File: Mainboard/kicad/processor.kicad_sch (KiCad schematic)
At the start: 74 parts, among them CON1 ICD15S13E4GV00LF, IC1 STM32F765ZGT6, J1 20021521-00010D4LF, J2 SH_CON, U1 24LC64, U2 MAX7375AXR805, U3 SZNUP4114HMR6T1G, U4 SZNUP4114HMR6T1G, U5 SZNUP4114HMR6T1G, U6 SZNUP4114HMR6T1G

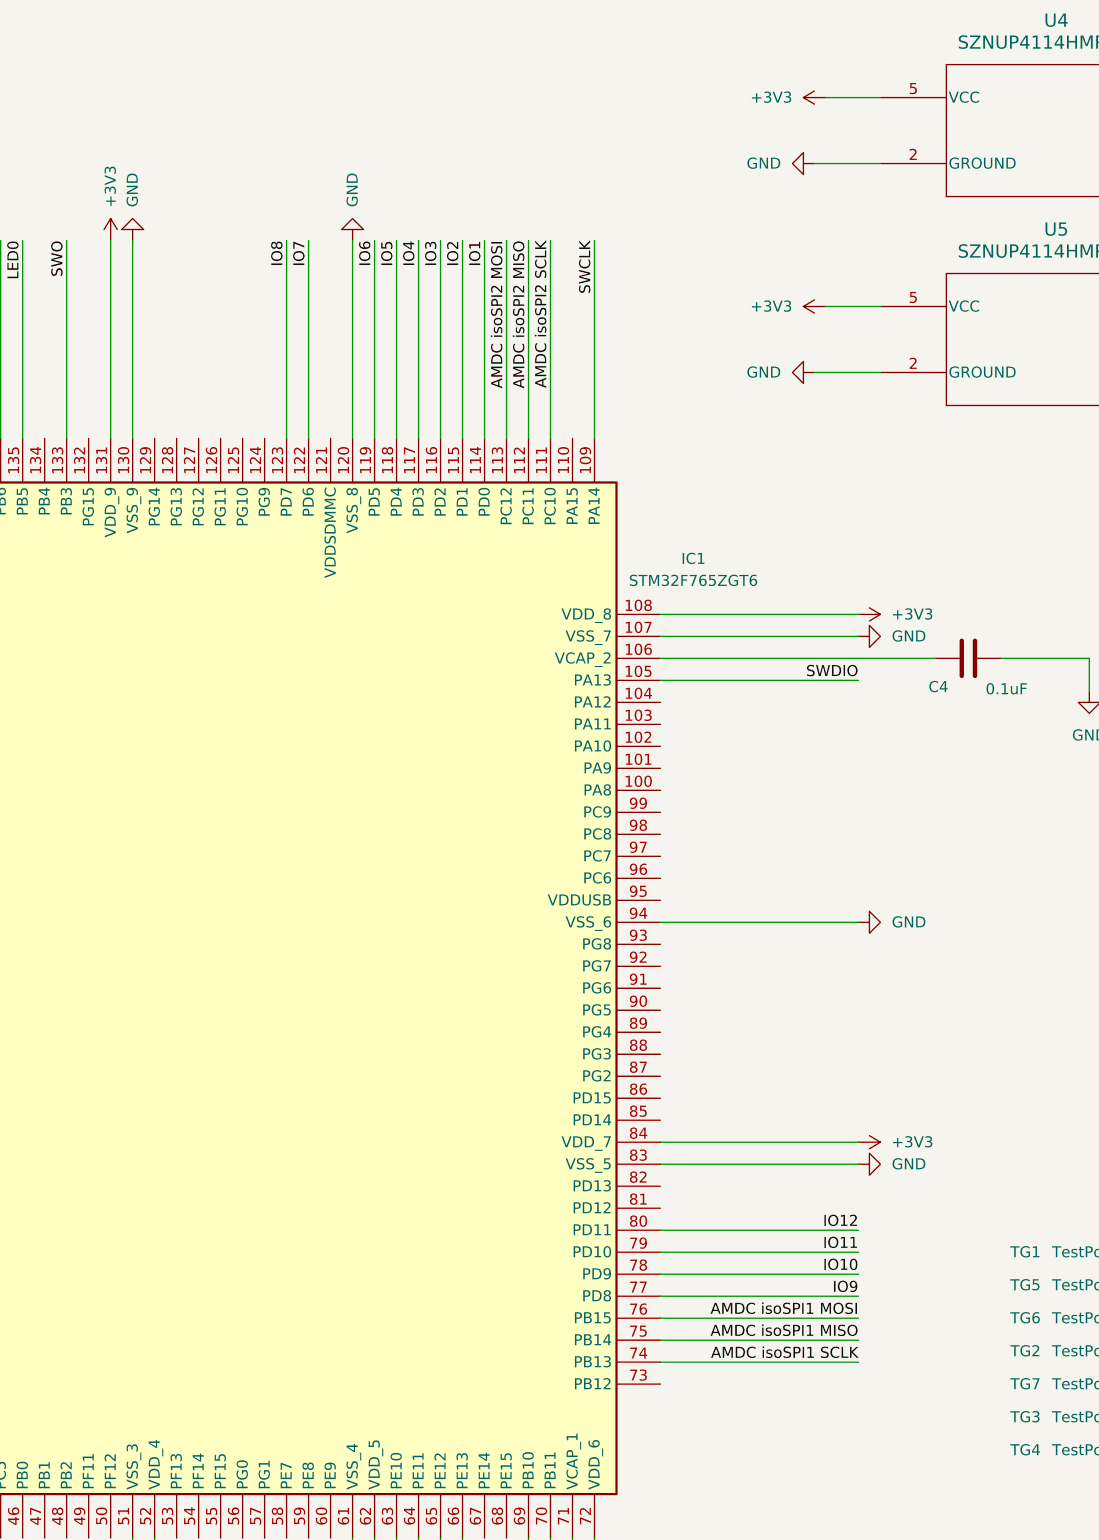
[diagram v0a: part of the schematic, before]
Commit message: Correct LED direction and processor pins
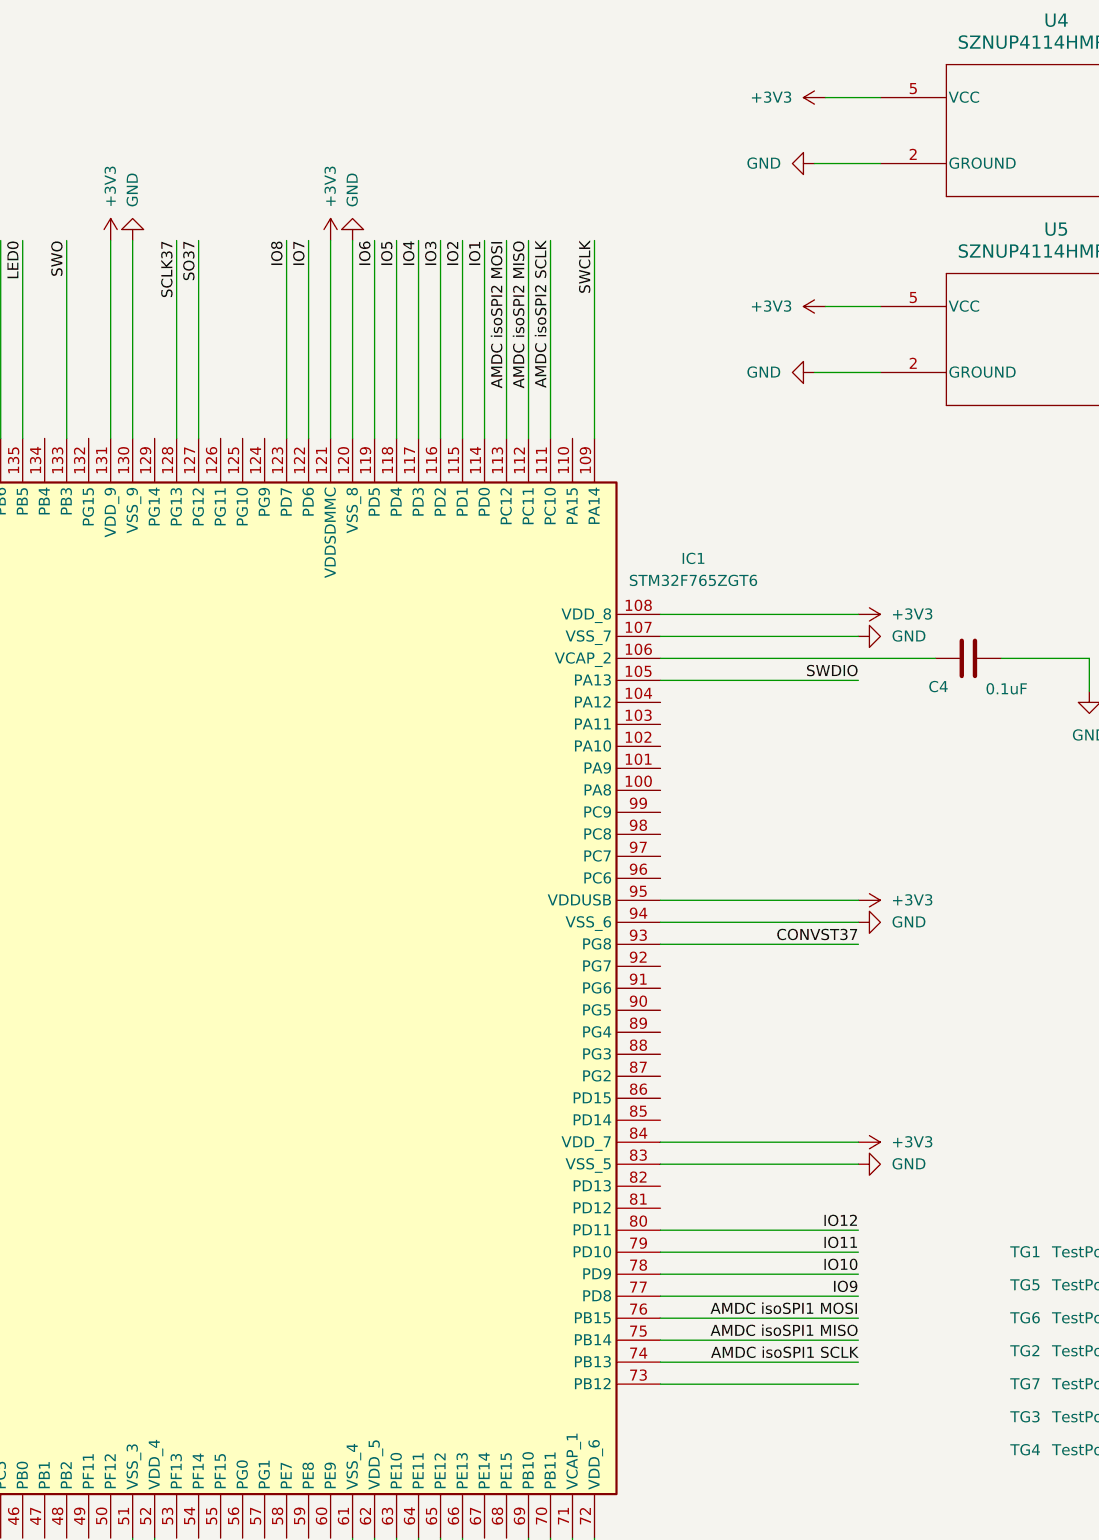
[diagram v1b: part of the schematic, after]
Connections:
- net +3V3: now also IC1.121 (VDDSDMMC), IC1.95 (VDDUSB)
- net CNVST37: now also IC1.93 (PG8)
- net SCLK37: now also IC1.128 (PG13)
- net SO37: now also IC1.127 (PG12)
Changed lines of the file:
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@@
 	(wire
 		(pts
+			(xy 264.16 198.12) (xy 287.02 198.12)
+		)
+		(stroke
+			(width 0)
+			(type default)
+		)
+	)
+	(wire
+		(pts
 			(xy 228.6 238.76) (xy 228.6 215.9)
 		)
@@
 	(wire
 		(pts
+			(xy 210.82 88.9) (xy 210.82 66.04)
+		)
+		(stroke
+			(width 0)
+			(type default)
+		)
+	)
+	(wire
+		(pts
 			(xy 220.98 88.9) (xy 220.98 66.04)
 		)
@@
 	(wire
 		(pts
+			(xy 287.02 147.32) (xy 264.16 147.32)
+		)
+		(stroke
+			(width 0)
+			(type default)
+		)
+	)
+	(wire
+		(pts
 			(xy 190.5 88.9) (xy 190.5 66.04)
 		)
@@
 	(wire
 		(pts
+			(xy 208.28 88.9) (xy 208.28 66.04)
+		)
+		(stroke
+			(width 0)
+			(type default)
+		)
+	)
+	(wire
+		(pts
 			(xy 64.77 261.62) (xy 64.77 269.24)
 		)
@@
 	(wire
 		(pts
+			(xy 226.06 88.9) (xy 226.06 66.04)
+		)
+		(stroke
+			(width 0)
+			(type default)
+		)
+	)
+	(wire
+		(pts
 			(xy 124.46 187.96) (xy 124.46 191.77)
 		)
@@
 	(wire
 		(pts
+			(xy 287.02 142.24) (xy 264.16 142.24)
+		)
+		(stroke
+			(width 0)
+			(type default)
+		)
+	)
+	(wire
+		(pts
 			(xy 48.26 115.57) (xy 58.42 115.57)
 		)
@@
 		)
 	)
+	(label "SCLK37"
+		(at 208.28 66.04 270)
+		(effects
+			(font
+				(size 1.27 1.27)
+			)
+			(justify right bottom)
+		)
+	)
 	(label "AMDC isoSPI2 SCLK"
 		(at 356.87 199.39 0)
@@
 		)
 	)
+	(label "CONVST37"
+		(at 287.02 147.32 180)
+		(effects
+			(font
+				(size 1.27 1.27)
+			)
+			(justify right bottom)
+		)
+	)
 	(label "AMDC isoSPI1 NSS"
 		(at 356.87 193.04 0)
@@
 		)
 	)
+	(label "SO37"
+		(at 210.82 66.04 270)
+		(effects
+			(font
+				(size 1.27 1.27)
+			)
+			(justify right bottom)
+		)
+	)
 	(label "IO1"
 		(at 339.09 54.61 180)
@@
 	(symbol
 		(lib_id "power:+3V3")
+		(at 287.02 142.24 270)
+		(unit 1)
+		(exclude_from_sim no)
+		(in_bom yes)
+		(on_board yes)
+		(dnp no)
+		(fields_autoplaced yes)
+		(property "Reference" "#PWR0190"
+			(at 283.21 142.24 0)
+			(effects
+				(font
+					(size 1.27 1.27)
+				)
+				(hide yes)
+			)
+		)
+		(property "Value" "+3V3"
+			(at 290.83 142.2401 90)
+			(effects
+				(font
+					(size 1.27 1.27)
+				)
+				(justify left)
+			)
+		)
+		(property "Footprint" ""
+			(at 287.02 142.24 0)
+			(effects
+				(font
+					(size 1.27 1.27)
+				)
+				(hide yes)
+			)
+		)
+		(property "Datasheet" ""
+			(at 287.02 142.24 0)
+			(effects
+				(font
+					(size 1.27 1.27)
+				)
+				(hide yes)
+			)
+		)
+		(property "Description" "Power symbol creates a global label with name \"+3V3\""
+			(at 287.02 142.24 0)
+			(effects
+				(font
+					(size 1.27 1.27)
+				)
+				(hide yes)
+			)
+		)
+		(pin "1"
+		)
+		(instances
+			(project "ST_MCU_and_Current_Sensing"
+				(path "/3118e6ec-7f2d-463d-8664-25fa12ba0e31/b44cb9df-cc81-42a2-af43-d93c559dd28a"
+					(reference "#PWR0190")
+					(unit 1)
+				)
+			)
+		)
+	)
+	(symbol
+		(lib_id "power:+3V3")
 		(at 256.54 233.68 180)
 		(unit 1)
@@
 					(unit 1)
 				)
+			)
+		)
+	)
+	(symbol
+		(lib_id "power:+3V3")
+		(at 226.06 66.04 0)
+		(unit 1)
+		(exclude_from_sim no)
+		(in_bom yes)
+		(on_board yes)
+		(dnp no)
+		(fields_autoplaced yes)
+		(property "Reference" "#PWR0189"
+			(at 226.06 69.85 0)
+			(effects
+				(font
+					(size 1.27 1.27)
+				)
+				(hide yes)
+			)
+		)
+		(property "Value" "+3V3"
+			(at 226.0601 62.23 90)
+			(effects
+				(font
+					(size 1.27 1.27)
+				)
+				(justify left)
+			)
+		)
+		(property "Footprint" ""
+			(at 226.06 66.04 0)
+			(effects
+				(font
+					(size 1.27 1.27)
+				)
+				(hide yes)
+			)
+		)
+		(property "Datasheet" ""
+			(at 226.06 66.04 0)
+			(effects
+				(font
+					(size 1.27 1.27)
+				)
+				(hide yes)
+			)
+		)
+		(property "Description" "Power symbol creates a global label with name \"+3V3\""
+			(at 226.06 66.04 0)
+			(effects
+				(font
+					(size 1.27 1.27)
+				)
+				(hide yes)
+			)
+		)
+		(pin "1"
+		)
+		(instances
+			(project "ST_MCU_and_Current_Sensing"
+				(path "/3118e6ec-7f2d-463d-8664-25fa12ba0e31/b44cb9df-cc81-42a2-af43-d93c559dd28a"
+					(reference "#PWR0189")
+					(unit 1)
+				)

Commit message: Finish schematic corrections
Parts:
- added R54: 0R, symbol Device:R_US
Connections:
- net AMDC isoSPI1 NSS: now also IC1.73 (PB12)
- net I2C SCL: now also IC1.11 (PF1)
- net SO26: now also R54.1
- net BUSY26: now reaches IC1.57 (PG1)
- net BUSY26: now also R54.2
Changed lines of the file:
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@@
 	(wire
 		(pts
+			(xy 218.44 246.38) (xy 218.44 234.95)
+		)
+		(stroke
+			(width 0)
+			(type default)
+		)
+	)
+	(wire
+		(pts
 			(xy 251.46 238.76) (xy 251.46 215.9)
 		)
@@
 	(wire
 		(pts
+			(xy 218.44 227.33) (xy 218.44 215.9)
+		)
+		(stroke
+			(width 0)
+			(type default)
+		)
+	)
+	(wire
+		(pts
 			(xy 35.56 193.04) (xy 41.91 193.04)
 		)
@@
 	(wire
 		(pts
+			(xy 137.16 134.62) (xy 160.02 134.62)
+		)
+		(stroke
+			(width 0)
+			(type default)
+		)
+	)
+	(wire
+		(pts
 			(xy 241.3 88.9) (xy 241.3 66.04)
 		)
@@
 		)
 	)
+	(label "BUSY26"
+		(at 218.44 227.33 90)
+		(effects
+			(font
+				(size 1.27 1.27)
+			)
+			(justify left bottom)
+		)
+	)
 	(label "IO3"
 		(at 358.14 31.75 0)
@@
 		)
 	)
+	(label "SO26"
+		(at 218.44 246.38 90)
+		(effects
+			(font
+				(size 1.27 1.27)
+			)
+			(justify left bottom)
+		)
+	)
 	(label "BUSY48"
 		(at 149.86 193.04 0)
@@
 		)
 	)
+	(label "AMDC isoSPI1 NSS"
+		(at 287.02 198.12 180)
+		(effects
+			(font
+				(size 1.27 1.27)
+			)
+			(justify right bottom)
+		)
+	)
 	(label "SCLK48"
 		(at 356.87 109.22 0)
@@
 		)
 	)
+	(label "I2C SCL"
+		(at 137.16 134.62 0)
+		(effects
+			(font
+				(size 1.27 1.27)
+			)
+			(justify left bottom)
+		)
+	)
 	(hierarchical_label "AMDC isoSPI1 MISO"
 		(shape output)
@@
 					(unit 1)
 				)
+			)
+		)
+	)
+	(symbol
+		(lib_id "Device:R_US")
+		(at 218.44 231.14 180)
+		(unit 1)
+		(exclude_from_sim no)
+		(in_bom yes)
+		(on_board yes)
+		(dnp no)
+		(property "Reference" "R54"
+			(at 219.964 235.712 90)
+			(effects
+				(font
+					(size 1.27 1.27)
+				)
+			)
+		)
+		(property "Value" "0R"
+			(at 219.964 225.806 90)
+			(effects
+				(font
+					(size 1.27 1.27)
+				)
+			)
+		)
+		(property "Footprint" ""
+			(at 217.424 230.886 90)
+			(effects
+				(font
+					(size 1.27 1.27)
+				)
+				(hide yes)
+			)
+		)
+		(property "Datasheet" "~"
+			(at 218.44 231.14 0)
+			(effects
+				(font
+					(size 1.27 1.27)
+				)
+				(hide yes)
+			)
+		)
+		(property "Description" "Resistor, US symbol"
+			(at 218.44 231.14 0)
+			(effects
+				(font
+					(size 1.27 1.27)
+				)
+				(hide yes)
+			)
+		)
+		(pin "2"
+		)
+		(pin "1"
+		)
+		(instances
+			(project "ST_MCU_and_Current_Sensing"
+				(path "/3118e6ec-7f2d-463d-8664-25fa12ba0e31/b44cb9df-cc81-42a2-af43-d93c559dd28a"
+					(reference "R54")
+					(unit 1)
+				)
